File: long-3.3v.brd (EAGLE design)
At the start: 50 x 50 mm, 37 parts, among them U1 USD-SOCKET, U2 MCP73831, U4 ADXL375BCCZ, X1 Micro USB, X2 CRYSTAL

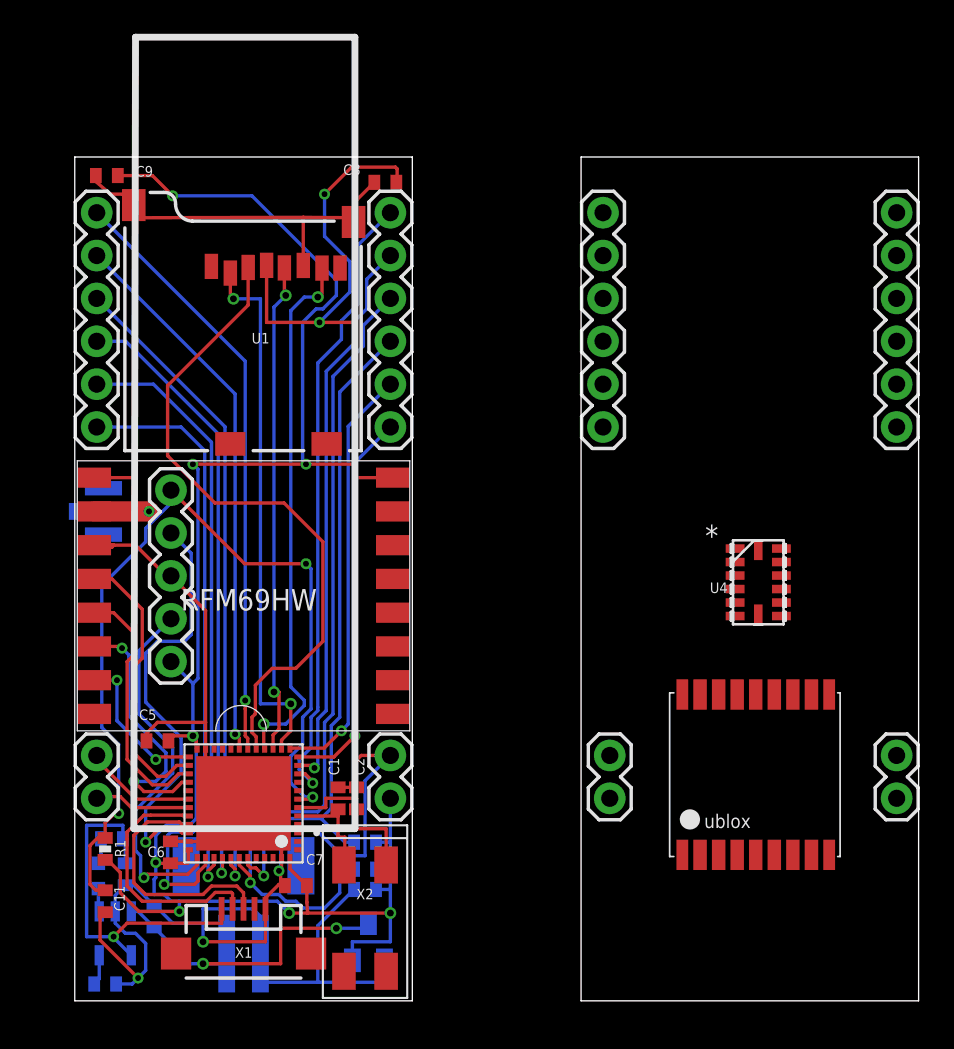
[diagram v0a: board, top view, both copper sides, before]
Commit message: Routed antenna in coplanar waveguide. Removed some other tracks to do it though. Matt's turn!
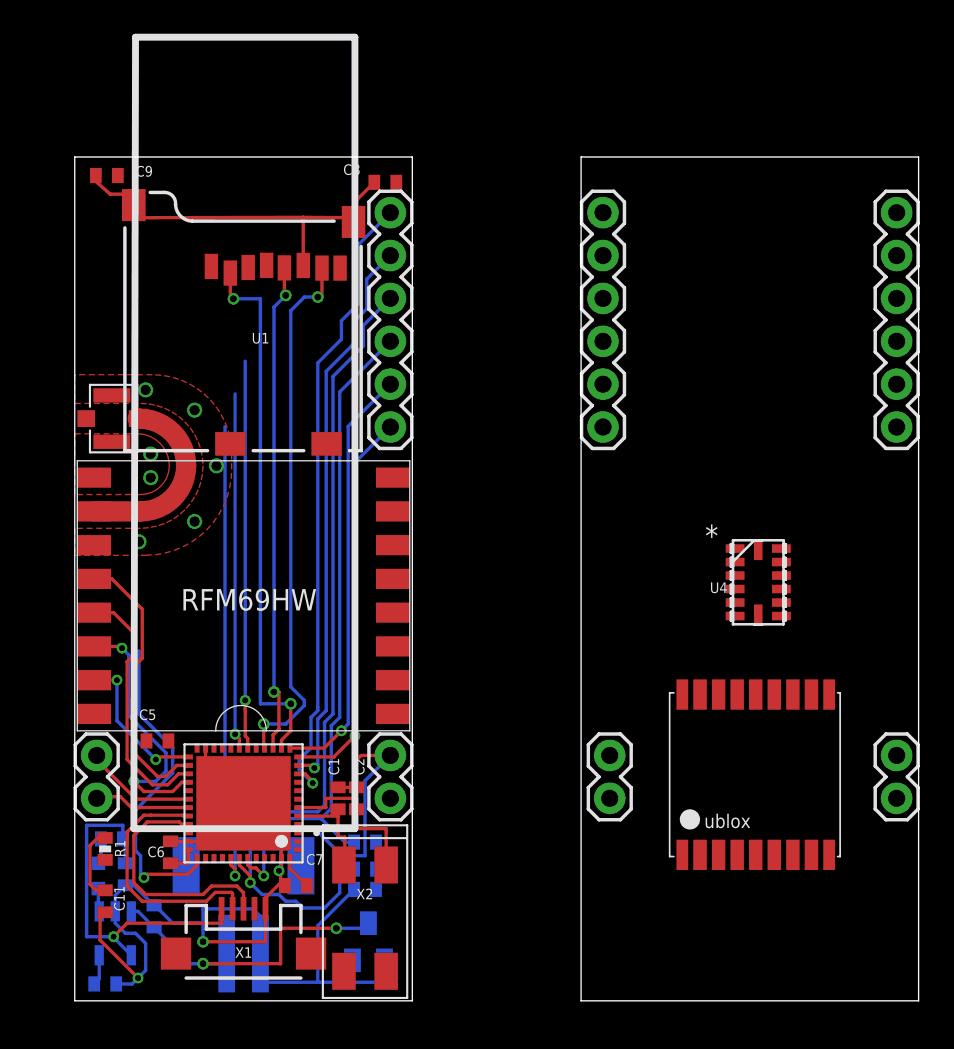
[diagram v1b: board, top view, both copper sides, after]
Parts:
- removed JP1: (no value), SparkFun:1X05
- removed JP10: (no value), SparkFun-Connectors:1X06
- moved U$4 5.52 mm to (2.20, 34.5), flipped to the top, turned to 0 degrees
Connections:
- net CS: no longer JP10.1
- net GND: no longer JP1.3
- net MISO: no longer JP10.3
- net MOSI: no longer JP10.4
- net NRST: no longer JP1.5
- net PB0: no longer JP10.6
- net PB1: no longer JP10.5
- net SCK: no longer JP10.2
- net SWCLK: no longer JP1.2
- net SWDIO: no longer JP1.4
- net VCC: no longer JP1.1
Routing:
- net VCC: track 146.3 -> 3.83 mm, vias 10 -> 0
- net NRST: track 53.6 -> 4.43 mm, vias 3 -> 0
- net GND: track 156.6 -> 113.1 mm, vias 3 -> 10
- net SD_MOSI: track 39.3 -> 0.00 mm
- net CS: track 38.0 -> 0.00 mm, vias 1 -> 0
- net MISO: track 36.4 -> 0.00 mm, vias 1 -> 0
- net SCK: track 35.3 -> 0.00 mm, vias 1 -> 0
- net SWDIO: track 25.6 -> 0.00 mm, vias 1 -> 0
- net PB0: track 35.4 -> 23.0 mm
- net PB1: track 32.7 -> 21.1 mm
- net MOSI: track 38.8 -> 28.1 mm
- net N$4: track 4.43 -> 10.6 mm, vias 1 -> 0
- net SWCLK: track 21.9 -> 19.2 mm
- added copper zone on layer 1, net GND

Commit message: Updated schematic, unrouted board Added temperature sensor, power switch, 32.768kHz crystal Changed 8MHz crystal Changed connections to micro
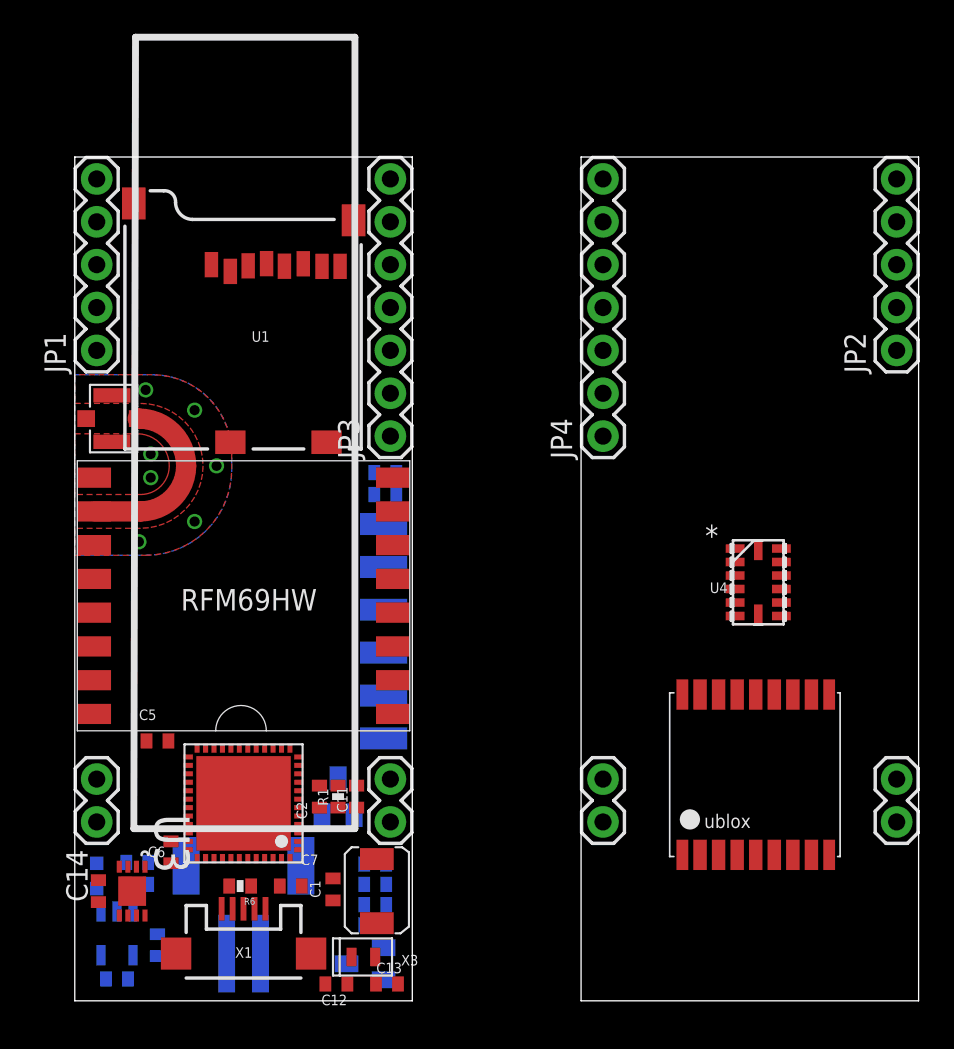
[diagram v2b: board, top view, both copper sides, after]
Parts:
- removed JP11, JP12, JP13: (no value), SparkFun-Connectors:1X06
- added C12, C13: 20pF, rcl:C0402
- added C14: 100nF, rcl:C0402
- added J1: CON_HEADER_1X06-SMD-RIGHT-ANGLED, dp_devices:M1X6_MALE_RIGHT_ANGLED_SMD
- added JP1, JP2: (no value), SparkFun:1X05
- added JP3, JP4: (no value), SparkFun:1X07
- added Q1: BSS84, transistor-small-signal:SOT23
- added R6: 0R, SparkFun:0402-RES
- added R7: 100k, SparkFun:0402-RES
- added U3: MCP9808T-E/MC, mattsLib:DFN300X200X100-9N
- added X3: CRYSTALS-NOGND-IQXC-25, IQD-Frequency-Products:2.0X1.2-2PAD
- R1: value 10k -> 100k
- X2: device IQD-Frequency-Products:7.5X5-4-PAD -> Ava:ABRACON_ABM3_CRYSTAL
- moved C9 24.1 mm to (18.4, 31.3), flipped to the bottom, turned to 0 degrees
- moved C8 18.5 mm to (18.4, 30.0), flipped to the bottom, turned to 0 degrees
- moved JP17 17.4 mm to (31.3, 13.1), turned to 270 degrees
- moved JP16 17.0 mm to (48.7, 13.1), turned to 270 degrees
- moved C11 16.1 mm to (16.7, 12.1), turned to 90 degrees
- moved R1 14.1 mm to (15.6, 12.1), turned to 270 degrees
- moved C1 5.41 mm to (15.3, 6.60), turned to 270 degrees
- moved X2 3.20 mm to (18.0, 8.00), turned to 90 degrees
- moved R5 2.57 mm to (17.8, 6.90)
- moved C2 2.20 mm to (14.5, 12.1)
- moved C10 2.18 mm to (17.8, 4.50)
- moved R2 2.18 mm to (17.8, 5.70)
- moved R3 2.05 mm to (3.70, 8.20)
- moved C4 1.71 mm to (4.90, 3.30)
- moved IC1 1.32 mm to (17.2, 2.20), turned to 270 degrees
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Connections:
- removed net CS: U$1.P$38
- removed net FC_RX: U$1.P$31
- removed net FC_TX: U$1.P$30
- removed net MISO: U$1.P$40
- removed net MOSI: U$1.P$41
- removed net PA0: JP11.6, U$1.P$10
- removed net PA1: JP11.5, U$1.P$11
- removed net PB0: U$1.P$18
- removed net PB1: U$1.P$19
- removed net RX: JP11.2, U$1.P$13
- removed net RX2: JP14.1
- removed net SCK: U$1.P$39
- removed net SCL: JP11.4, R2.2, U$1.P$42, U4.14
- removed net SDA: JP11.3, R5.2, U$1.P$43, U4.13
- removed net SPI_CS: JP13.1
- removed net SPI_MISO: JP13.3
- removed net SPI_MOSI: JP13.4
- removed net SPI_SCK: JP13.2
- removed net TX: JP11.1, U$1.P$12
- removed net TX2: JP14.2
- removed net VIN: C3.1, R3.2, U2.4, X1.VBUS
- new net BOOT0: R6.1, U$1.P$44
- new net EXT_CS: JP1.5, JP2.5, U$1.P$14
- new net EXT_MISO: JP1.3, JP2.3, U$1.P$40
- new net EXT_MOSI: JP1.2, JP2.2, U$1.P$41
- new net EXT_RX: JP3.6, U$1.P$13
- new net EXT_SCK: JP1.4, JP2.4, U$1.P$25
- new net EXT_SW: Q1.1, R7.2, U$1.P$2
- new net EXT_TX: JP3.7, U$1.P$12
- new net LOCAL_SCL: U$1.P$21, U3.2
- new net LOCAL_SDA: U$1.P$39, U3.1
- new net N$6: C13.1, U$1.P$4, X3.2
- new net N$7: C12.1, U$1.P$3, X3.1
- new net RADIO_DATA: U$1.P$29, U$3.DIO2
- new net VBUS: C3.1, R3.2, U$1.P$30, U2.4, X1.VBUS
- new net VCC_SW: JP15.1, JP17.1, Q1.3
- net GND: now also C12.2, C13.2, C14.2, J1.3, R6.2, U$1.P$8, U1.CD2, U3.4, U3.9
- net GPIO1: now also JP3.1, JP4.1, U$1.P$10; no longer JP12.6
- net GPIO2: now also JP3.2, JP4.2, U$1.P$11; no longer JP12.5
- net GPIO3: now also JP3.3, JP4.3, U$1.P$18; no longer JP13.6
- net GPIO4: now also JP1.1, JP2.1, U$1.P$19; no longer JP13.5
- net GPS_RX: now also JP14.2, U$1.P$42
- net GPS_TX: now also JP14.1, U$1.P$31
- net I2C_SCL: now also JP3.4, JP4.4, R2.2, U$1.P$45, U4.14; no longer JP12.4
- net I2C_SDA: now also JP3.5, JP4.5, R5.2, U$1.P$43, U4.13; no longer JP12.3
- net N$1: now also X2.P$1; no longer X2.1
- net N$2: now also X2.P$2; no longer X2.4
- net NRST: now also J1.5
- net RADIO_CS: now also U$1.P$46; no longer U$1.P$25
- net SD_CS: now also U$1.P$38; no longer U$1.P$14
- net SWCLK: now also J1.2
- net SWDIO: now also J1.4
- net UART_RX: now also JP4.6; no longer JP12.2
- net UART_TX: now also JP4.7; no longer JP12.1
- net VCC: now also C14.1, J1.1, Q1.2, R7.1, U$1.P$1, U$1.P$9, U3.5, U3.6, U3.7, U3.8; no longer JP15.1, JP17.1
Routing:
- net GND: track 113.1 -> 0.00 mm, vias 10 -> 7
- net SCL: track 49.4 -> 0.00 mm, vias 1 -> 0
- net SDA: track 40.2 -> 0.00 mm, vias 1 -> 0
- net PA0: track 37.5 -> 0.00 mm, vias 1 -> 0
- net PA1: track 33.2 -> 0.00 mm, vias 1 -> 0
- net SD_MISO: track 32.0 -> 0.00 mm, vias 2 -> 0
- net SD_CS: track 32.0 -> 0.00 mm, vias 2 -> 0
- net SD_SCK: track 29.3 -> 0.00 mm, vias 2 -> 0
- net MOSI: track 28.1 -> 0.00 mm, vias 1 -> 0
- net RX: track 25.2 -> 0.00 mm, vias 1 -> 0
- net TX: track 23.0 -> 0.00 mm, vias 1 -> 0
- net PB0: track 23.0 -> 0.00 mm, vias 1 -> 0
- net VIN: track 22.3 -> 0.00 mm, vias 1 -> 0
- net PB1: track 21.1 -> 0.00 mm, vias 1 -> 0
- net VBAT: track 19.7 -> 0.00 mm, vias 2 -> 0
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- added copper zone on layer 16, net GND
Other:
- board text removed: "CS"
- board text removed: "MISO"
- board text removed: "MOSI"
- board text removed: "PA0"
- board text removed: "PA1"
- board text removed: "PB0"
- board text removed: "PB1"
- board text removed: "RX"
- board text removed: "SCK"
- board text removed: "SCL"
- board text removed: "SDA"
- board text removed: "TX"

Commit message: Routed all the things (main board)
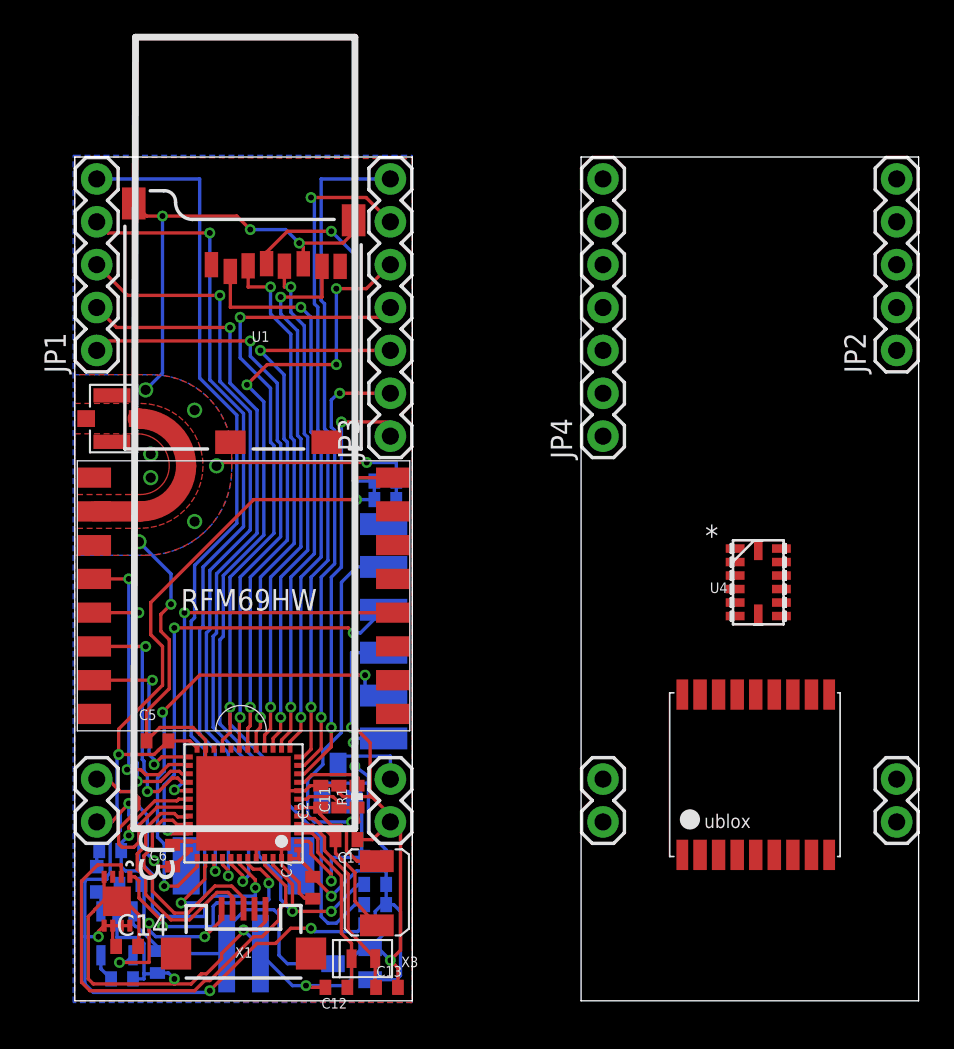
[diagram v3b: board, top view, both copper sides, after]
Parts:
- removed R6: 0R, SparkFun:0402-RES
- moved C14 3.69 mm to (3.10, 3.23), turned to 0 degrees
- moved C1 3.06 mm to (16.1, 9.55), turned to 0 degrees
- moved R3 1.75 mm to (2.10, 8.90)
- moved C7 1.30 mm to (14.1, 6.70), turned to 270 degrees
- moved R1 1.13 mm to (16.7, 12.1)
- moved U3 1.08 mm to (2.50, 5.90)
- moved C11 1.05 mm to (15.7, 12.1)
- moved C4 1.00 mm to (4.90, 2.30), turned to 270 degrees
- moved IC1 0.80 mm to (16.4, 2.20)
- moved Q1 0.80 mm to (15.6, 12.9)
- moved C9 0.50 mm to (18.4, 30.8), turned to 180 degrees
- moved C3 0.40 mm to (3.30, 6.90)
- moved R7 0.40 mm to (17.8, 8.50)
- moved C8 0.30 mm to (18.4, 29.7), turned to 180 degrees
- moved R4 0.30 mm to (2.80, 1.30)
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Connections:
- removed net BOOT0: R6.1, U$1.P$44
- net EXT_CS: now also U$1.P$38; no longer U$1.P$14
- net EXT_SCK: now also U$1.P$39; no longer U$1.P$25
- net GND: now also U$1.P$44; no longer R6.2
- net I2C_SCL: now also U$1.P$21; no longer U$1.P$45
- net I2C_SDA: now also U$1.P$46; no longer U$1.P$43
- net LOCAL_SCL: now also U$1.P$45; no longer U$1.P$21
- net LOCAL_SDA: now also U$1.P$43; no longer U$1.P$39
- net RADIO_CS: now also U$1.P$25; no longer U$1.P$46
- net SD_CS: now also U$1.P$14; no longer U$1.P$38
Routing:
- net GND: track 0.00 -> 161.1 mm, vias 7 -> 17
- net VCC: track 0.00 -> 141.7 mm, vias 0 -> 10
- net I2C_SDA: track 0.00 -> 57.1 mm, vias 0 -> 5
- net EXT_CS: track 0.00 -> 55.8 mm, vias 0 -> 1
- net I2C_SCL: track 0.00 -> 54.6 mm, vias 0 -> 2
- net EXT_SCK: track 0.00 -> 47.9 mm, vias 0 -> 2
- net EXT_MISO: track 0.00 -> 46.0 mm, vias 0 -> 2
- net EXT_MOSI: track 0.00 -> 45.6 mm, vias 0 -> 2
- net EXT_TX: track 0.00 -> 39.4 mm, vias 0 -> 1
- net EXT_RX: track 0.00 -> 38.9 mm, vias 0 -> 2
- net GPIO4: track 0.00 -> 35.2 mm, vias 0 -> 2
- net SD_CS: track 0.00 -> 33.6 mm, vias 0 -> 2
- net GPIO3: track 0.00 -> 32.9 mm, vias 0 -> 2
- net SD_MISO: track 0.00 -> 32.4 mm, vias 0 -> 2
- net SD_MOSI: track 0.00 -> 31.4 mm, vias 0 -> 2
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
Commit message: Switched from SD card to Flash memory
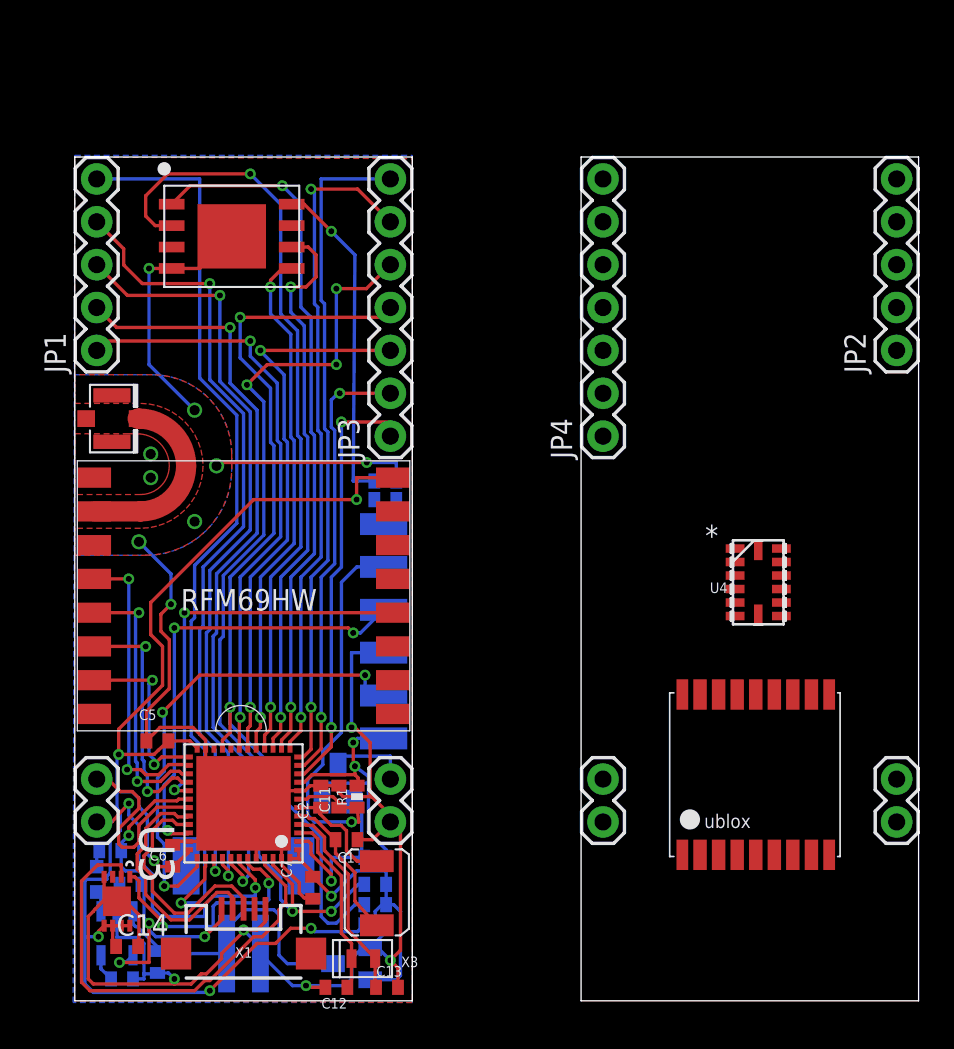
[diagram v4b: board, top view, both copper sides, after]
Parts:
- removed U1: USD-SOCKET, SparkFun-Connectors:MICROSD_1:1
- added U$5: S25FL256, mattsLib:WSON-8
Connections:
- removed net SD_CS: U$1.P$14, U1.2
- removed net SD_MISO: U$1.P$16, U1.7
- removed net SD_MOSI: U$1.P$17, U1.3
- removed net SD_SCK: U$1.P$15, U1.5
- new net FLASH_CS: U$1.P$14, U$5.P$1
- new net FLASH_MISO: U$1.P$16, U$5.P$2
- new net FLASH_MOSI: U$1.P$17, U$5.P$5
- new net FLASH_SCK: U$1.P$15, U$5.P$6
- net GND: now also U$5.P$4, U$5.P$9; no longer U1.6, U1.CD2, U1.GND1, U1.GND3
- net VCC: now also U$5.P$8; no longer U1.4
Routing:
- net FLASH_MISO: track 0.00 -> 45.9 mm, vias 0 -> 2
- net FLASH_CS: track 0.00 -> 41.9 mm, vias 0 -> 2
- net SD_CS: track 33.6 -> 0.00 mm, vias 2 -> 0
- net FLASH_SCK: track 0.00 -> 33.3 mm, vias 0 -> 2
- net SD_MISO: track 32.4 -> 0.00 mm, vias 2 -> 0
- net SD_MOSI: track 31.4 -> 0.00 mm, vias 2 -> 0
- net FLASH_MOSI: track 0.00 -> 30.8 mm, vias 0 -> 2
- net SD_SCK: track 30.2 -> 0.00 mm, vias 2 -> 0
- net GND: track 161.1 -> 148.2 mm, vias 17 -> 14
- net VCC: track 141.7 -> 137.5 mm
- net EXT_SCK: track 47.9 -> 46.7 mm
- net EXT_RX: track 38.9 -> 39.6 mm
